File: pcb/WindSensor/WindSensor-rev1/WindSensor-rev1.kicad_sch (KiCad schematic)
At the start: 14 parts, among them U1 Sensor_Wind, U2 Sensor_Wind, U3 Sensor_Wind, U4 LP5814DRLR

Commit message: update library parts for wind sensor
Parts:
- U4: symbol LP5814DRLR:LP5814DRLR -> WindSensor:LP5814DRLR
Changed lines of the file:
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@@
 	)
 	(symbol
-		(lib_id "LP5814DRLR:LP5814DRLR")
+		(lib_id "WindSensor:LP5814DRLR")
 		(at 143.51 68.58 0)
 		(unit 1)

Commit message: getting there
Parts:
- removed C2, C3: C_Small, Capacitor_SMD:C_0201_0603Metric, symbol Device:C_Small
- removed D1, D2, D3, D4: LED, WindSensor:LED_3528, symbol Device:LED
- removed R3: R_Small_US, Resistor_SMD:R_0201_0603Metric, symbol Device:R_Small_US
- added J1: Conn_I2C_Molex_705450003, WindSensor:CONN_SD-74099-1000_04_MOL, symbol WindSensor:Conn_I2C_Molex_740990604
- added LED1: 599-2310-427F, WindSensor:599-2310_DIA, symbol WindSensor:599-2310-427F
- added TP1, TP2, TP3, TP4: TestPoint_Probe_autonamed, argo:TestPoint_scope_probe_autonamed, symbol argo:TestPoint_Probe_autonamed
- C1: value C_Small -> 10u; footprint Capacitor_SMD:C_0201_0603Metric -> Capacitor_SMD:C_0603_1608Metric_Pad1.08x0.95mm_HandSolder
- R1: value R_US -> 1.2k; footprint Resistor_SMD:R_0201_0603Metric -> Resistor_SMD:R_0603_1608Metric_Pad0.98x0.95mm_HandSolder
- R2: value R_US -> 2.7k; footprint Resistor_SMD:R_0201_0603Metric -> Resistor_SMD:R_0603_1608Metric_Pad0.98x0.95mm_HandSolder
- U1: value Sensor_Wind -> SDP320x21
- U2: value Sensor_Wind -> SDP320x22
- U3: value Sensor_Wind -> SDP320x23
- U4: footprint LP5814DRLR:IC_LP5814DRLR -> WindSensor:IC_LP5814DRLR; Product page (none) -> https://www.ti.com/product/LP5814
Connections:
- net GND: now also C1.2, U1.17 (GND), U1.18 (GND), U2.17 (GND), U2.18 (GND), U3.17 (GND), U3.18 (GND), J1.4 (GND), TP1.1; no longer C1.1, U4.5 (OUT3)
- net SCL: now also J1.1 (SCLK), TP3.1
- net SDA: now also J1.2 (SDA), TP4.1
- net VDD: now also C1.1, J1.3 (5V), LED1.3, LED1.5, LED1.6, LED1.8, TP2.1; no longer C1.2
- net G: now reaches U4.7 (OUT1)
- net G: now also LED1.9
- net B: now reaches U4.6 (OUT2)
- net B: now also LED1.4
- net R: now reaches U4.8 (OUT0)
- net R: now also LED1.7
- new net W: LED1.2, U4.5 (OUT3)
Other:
- moved on the sheet: R1, R2, U1, U2, U3, U4

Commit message: rules
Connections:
- net VDD: now also LED1.1
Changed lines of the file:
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@@
+	)
+	(junction
+		(at 191.77 77.47)
+		(diameter 0)
+		(color 0 0 0 0)
 	)
 	(junction
@@
 		)
 		(stroke
+			(width 0)
+			(type default)
+		)
+	)
+	(wire
+		(pts
+			(xy 191.77 77.47) (xy 191.77 82.55)
+		)
+		(stroke

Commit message: centered, retrouted, cleaned up windsensor rev1
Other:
- note added: "VDD=5V"
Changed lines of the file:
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@@
 	(generator_version "9.0")
 	(paper "A5")
+	(text "VDD=5V"
+		(exclude_from_sim no)
+		(at 75.946 32.004 0)
+		(effects
+			(font
+				(size 3 3)
+			)
+		)
+	)
 	(junction
 		(at 59.69 73.66)

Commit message: add digikey info, update i2c header for wind sensor, made digikey order
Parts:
- added C1: 22u 16V, Capacitor_SMD:C_1210_3225Metric_Pad1.33x2.70mm_HandSolder, symbol Device:C
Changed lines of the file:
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@@
+	)
+	(symbol
+		(lib_id "Device:C")
+		(at 102.87 57.15 180)
+		(unit 1)
+		(exclude_from_sim no)
+		(in_bom yes)
+		(on_board yes)
+		(dnp no)
+		(property "Reference" "C1"
+			(at 100.584 59.436 0)
+			(effects
+				(font
+					(size 1.27 1.27)
+				)
+			)
+		)
+		(property "Value" "22u 16V"
+			(at 107.442 54.61 0)
+			(effects
+				(font
+					(size 1.27 1.27)
+				)
+			)
+		)
+		(property "Footprint" "Capacitor_SMD:C_1210_3225Metric_Pad1.33x2.70mm_HandSolder"
+			(at 101.9048 53.34 0)
+			(effects
+				(font
+					(size 1.27 1.27)
+				)
+				(hide yes)
+			)
+		)
+		(property "Datasheet" "https://content.kemet.com/datasheets/KEM_C1006_X5R_SMD.pdf"
+			(at 102.87 57.15 0)
+			(effects
+				(font
+					(size 1.27 1.27)
+				)
+				(hide yes)
+			)
+		)
+		(property "Description" "Unpolarized capacitor"
+			(at 102.87 57.15 0)
+			(effects
+				(font
+					(size 1.27 1.27)
+				)
+				(hide yes)
+			)
+		)
+		(property "Order" "https://ch.farnell.com/en-CH/kemet/c1210c226k4pactu/cap-22-f-16v-10-x5r-1210/dp/1288266"
+			(at 102.87 57.15 0)
+			(effects
+				(font
+					(size 1.27 1.27)
+				)
+				(hide yes)
+			)
+		)
+		(property "digikey" "https://www.digikey.ch/en/products/detail/kemet/c1210c226k4pactu/1465597"
+			(at 102.87 57.15 0)
+			(effects
+				(font
+					(size 1.27 1.27)
+				)
+				(hide yes)
+			)
+		)
+		(pin "1"
+		)
+		(pin "2"
+		)
+		(instances
+			(project "WindSensor-rev1"
+				(path "/094e312f-2c62-41df-b67d-51e0bb0b4171"
+					(reference "C1")
+					(unit 1)
+				)
+			)
+		)
 	)
 	(symbol

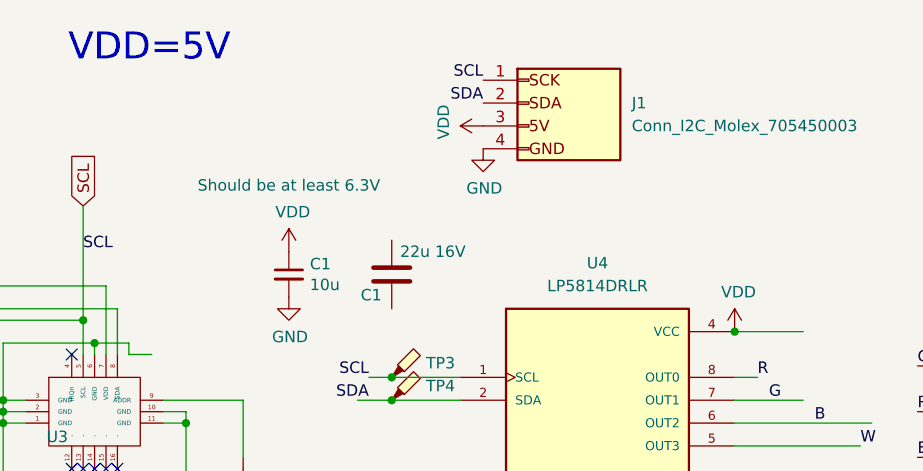
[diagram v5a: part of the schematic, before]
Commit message: changed cap to 22uF used on argo pcb. removed v0 pcb from this folder. latest versions of 3d design. case and start of first air channel. step for SDP32 might be missing.
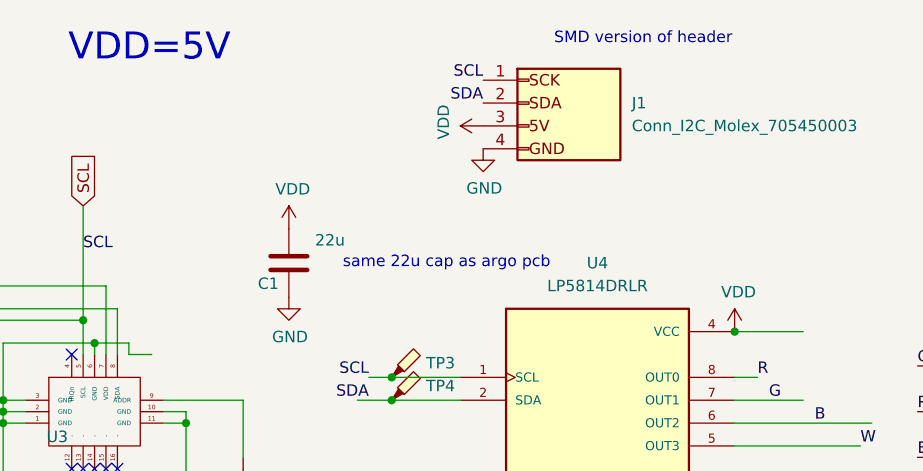
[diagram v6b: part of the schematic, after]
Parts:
- removed C1: 10u, Capacitor_SMD:C_0603_1608Metric_Pad1.08x0.95mm_HandSolder, symbol Device:C_Small
- C1: value 22u 16V -> 22u
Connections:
- net GND: now also C1.1
- net VDD: now also C1.2
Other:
- note added: "SMD version of header"
- note added: "same 22u cap as argo pcb"
- moved on the sheet: C1
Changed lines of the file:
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@@
 		)
 	)
+	(text "same 22u cap as argo pcb"
+		(exclude_from_sim no)
+		(at 108.966 55.88 0)
+		(effects
+			(font
+				(size 1.27 1.27)
+			)
+		)
+	)
+	(text "SMD version of header"
+		(exclude_from_sim no)
+		(at 130.81 30.988 0)
+		(effects
+			(font
+				(size 1.27 1.27)
+			)
+		)
+	)
 	(junction
 		(at 59.69 73.66)
@@
 	(symbol
 		(lib_id "Device:C")
-		(at 102.87 57.15 180)
+		(at 91.44 55.88 180)
 		(unit 1)
 		(exclude_from_sim no)
@@
 		(dnp no)
 		(property "Reference" "C1"
-			(at 100.584 59.436 0)
+			(at 89.154 58.166 0)
 			(effects
 				(font
@@
 			)
 		)
-		(property "Value" "22u 16V"
-			(at 107.442 54.61 0)
+		(property "Value" "22u"
+			(at 96.012 53.34 0)
 			(effects
 				(font
@@
 		)
 		(property "Footprint" "Capacitor_SMD:C_1210_3225Metric_Pad1.33x2.70mm_HandSolder"
-			(at 101.9048 53.34 0)
+			(at 90.4748 52.07 0)
 			(effects
 				(font
@@
 		)
 		(property "Datasheet" "https://content.kemet.com/datasheets/KEM_C1006_X5R_SMD.pdf"
-			(at 102.87 57.15 0)
+			(at 91.44 55.88 0)
 			(effects
 				(font
@@
 		)
 		(property "Description" "Unpolarized capacitor"
-			(at 102.87 57.15 0)
+			(at 91.44 55.88 0)
 			(effects
 				(font
@@
 		)
 		(property "Order" "https://ch.farnell.com/en-CH/kemet/c1210c226k4pactu/cap-22-f-16v-10-x5r-1210/dp/1288266"
-			(at 102.87 57.15 0)
+			(at 91.44 55.88 0)
 			(effects
 				(font
@@
 		)
 		(property "digikey" "https://www.digikey.ch/en/products/detail/kemet/c1210c226k4pactu/1465597"
-			(at 102.87 57.15 0)
+			(at 91.44 55.88 0)
 			(effects
 				(font
@@
 	)
 	(symbol
-		(lib_id "Device:C_Small")
-		(at 91.44 57.15 0)
-		(unit 1)
-		(exclude_from_sim no)
-		(in_bom yes)
-		(on_board yes)
-		(dnp no)
-		(property "Reference" "C1"
-			(at 93.7768 55.9816 0)
-			(effects
-				(font
-					(size 1.27 1.27)
-				)
-				(justify left)
-			)
-		)
-		(property "Value" "10u"
-			(at 93.7768 58.293 0)
-			(effects
-				(font
-					(size 1.27 1.27)
-				)
-				(justify left)
-			)
-		)
-		(property "Footprint" "Capacitor_SMD:C_0603_1608Metric_Pad1.08x0.95mm_HandSolder"
-			(at 91.44 57.15 0)
-			(effects
-				(font
-					(size 1.27 1.27)
-				)
-				(hide yes)
-			)
-		)
-		(property "Datasheet" "~"
-			(at 91.44 57.15 0)
-			(effects
-				(font
-					(size 1.27 1.27)
-				)
-				(hide yes)
-			)
-		)
-		(property "Description" "Should be at least 6.3V"
-			(at 91.44 47.244 0)
-			(effects
-				(font
-					(size 1.27 1.27)
-				)
-			)
-		)
-		(pin "1"
-		)
-		(pin "2"
-		)
-		(instances
-			(project "WindSensor-rev1"
-				(path "/094e312f-2c62-41df-b67d-51e0bb0b4171"
-					(reference "C1")
-					(unit 1)
-				)
-			)
-		)
-	)
-	(symbol
 		(lib_id "WindSensor:599-2310-427F")
 		(at 161.29 67.31 0)
@@
 	(symbol
 		(lib_id "power:VDD")
-		(at 91.44 54.61 0)
+		(at 91.44 52.07 0)
 		(unit 1)
 		(exclude_from_sim no)
@@
 		(dnp no)
 		(property "Reference" "#PWR06"
-			(at 91.44 58.42 0)
+			(at 91.44 55.88 0)
 			(effects
 				(font
@@
 		)
 		(property "Value" "VDD"
-			(at 91.8718 50.2158 0)
+			(at 91.8718 47.6758 0)
 			(effects
 				(font
@@
 		)
 		(property "Footprint" ""
-			(at 91.44 54.61 0)
+			(at 91.44 52.07 0)
 			(effects
 				(font
@@
 		)
 		(property "Datasheet" ""
-			(at 91.44 54.61 0)
+			(at 91.44 52.07 0)
 			(effects
 				(font
@@
 		)
 		(property "Description" ""
-			(at 91.44 54.61 0)
+			(at 91.44 52.07 0)
 			(effects
 				(font

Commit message: finally a version of case design that is getting close to fab. Plus some minor PCB updates to change cap to 10uF, fix labels.
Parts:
- LED1: footprint WindSensor:599-2310_DIA -> WindSensor:599-2310_DIA_hand_solder
- U4: footprint WindSensor:IC_LP5814DRLR -> WindSensor:IC_LP5814DRLR_hand_solder
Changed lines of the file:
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@@
 			)
 		)
-		(property "Footprint" "WindSensor:IC_LP5814DRLR"
+		(property "Footprint" "WindSensor:IC_LP5814DRLR_hand_solder"
 			(at 125.73 71.12 0)
 			(effects
@@
 			)
 		)
-		(property "Footprint" "WindSensor:599-2310_DIA"
+		(property "Footprint" "WindSensor:599-2310_DIA_hand_solder"
 			(at 161.29 67.31 0)
 			(effects

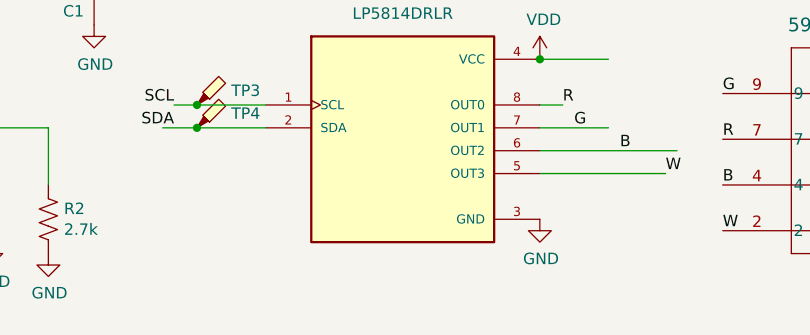
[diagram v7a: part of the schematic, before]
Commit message: add LP5814DLR I2C address 0x2C
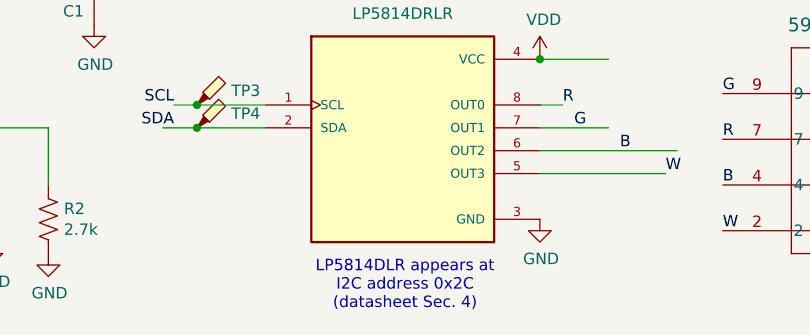
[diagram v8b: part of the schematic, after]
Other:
- note added: "LP5814DLR appears at I2C address 0x2C (datasheet Sec. 4)"
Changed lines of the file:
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@@
+		)
+	)
+	(text "LP5814DLR appears at\nI2C address 0x2C\n(datasheet Sec. 4)"
+		(exclude_from_sim no)
+		(at 125.984 88.646 0)
+		(effects
+			(font
+				(size 1.27 1.27)
+			)
 		)
 	)
